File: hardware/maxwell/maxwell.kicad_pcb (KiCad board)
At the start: 2 copper layers, 122 x 59 mm, 99 parts, among them J1 Canbus 1, J10 SPI2_B, J11 BACKUP, J12 UART4, J13 UART5, J14 I2C1, J16 ESP_BM, J17 ESP_PROG, J19 Interconnect (Power), J2 SPI2_C, J20 Interconnect (uC), J3 Neopixel, J4 BOOT0, J5 SPI2_A, J6 Programmer, J7 Dynamo Input, J8 BOOT1, J9 Battery, Q1 BSS138, Q2 PSMN5R4-25YLD, Q3 DMG9926UDM, Q4 NTR1P02T1, Q5 NTR1P02T1, U1 MCP1501, U10 MIC39102, U11 AP9101C-SOT-25, U12 INA219AID, U13 PCF8593, U2 SN65HVD233, U3 TPS2113, U4 PCA9536D, U5 ESP-32S, U6 AD7991, U7 STM32F103RETx, U8 TLP188, U9 Buck Regulator, Y1 32.768k, Y2 8M

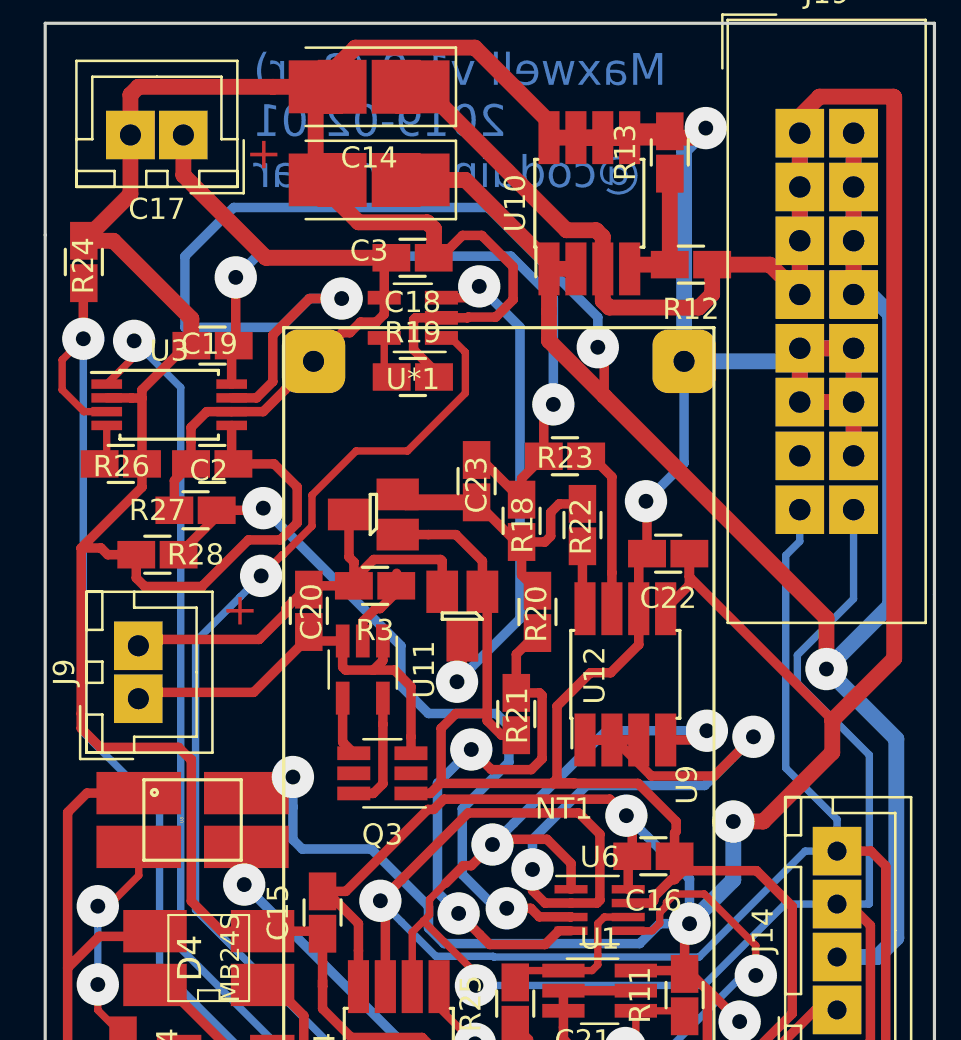
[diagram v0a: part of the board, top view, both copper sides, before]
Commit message: Updating to 1.8b; re-assigns power sources-to-TPS chip reverting earlier changes.
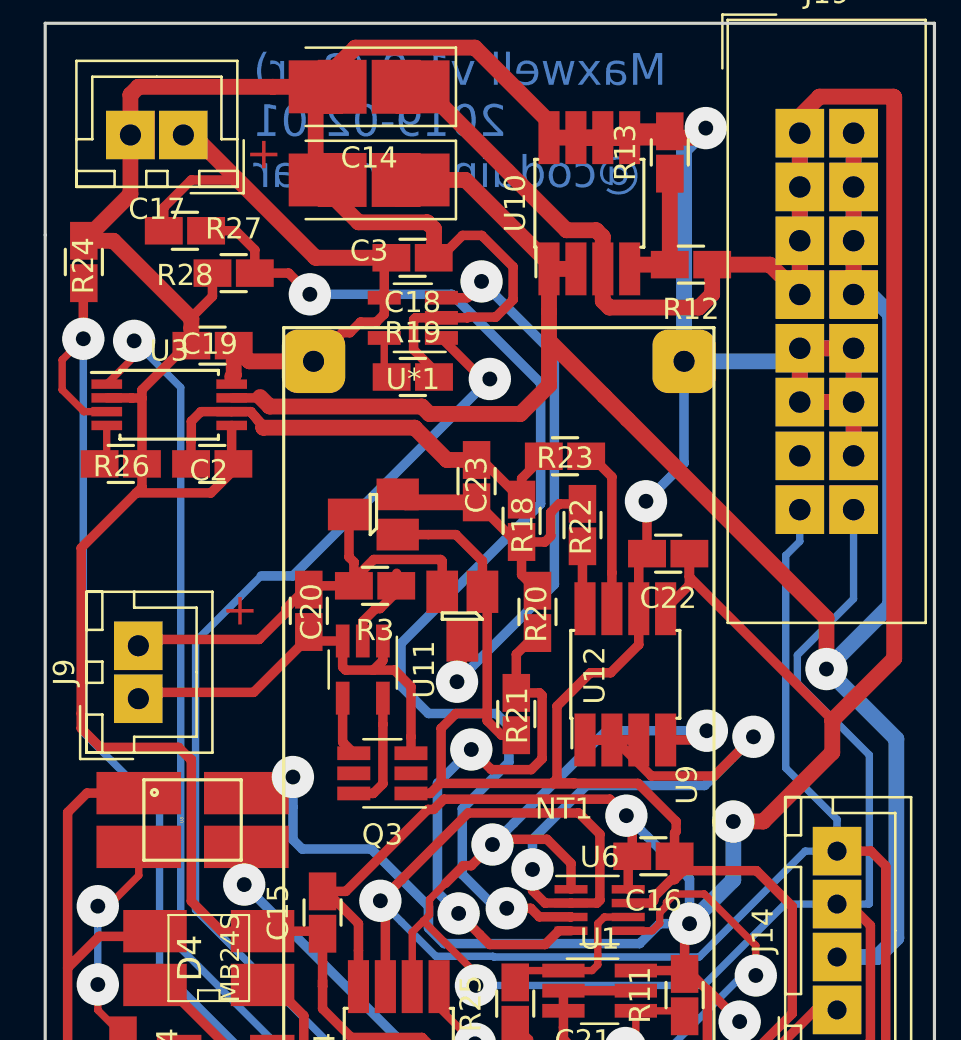
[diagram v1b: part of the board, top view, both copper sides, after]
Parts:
- moved R27 13.8 mm to (65.9, 84.8)
- moved R28 13.2 mm to (63.6, 82.8)
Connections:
- net DISABLE_DYNAMO_SRC renamed DISABLE_BATTERY_SRC
- C19 pad 2: +BATT -> /Power/+Dynamo_Buck
- C2 pad 1: /Power/+Dynamo_Buck -> +BATT
- U3 pad 6: /Power/+Dynamo_Buck -> +BATT
- U3 pad 8: +BATT -> /Power/+Dynamo_Buck
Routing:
- net VCC: track 325.6 -> 297.4 mm, vias 3 -> 1
- net DYNAMO_REG_VOLTAGE: track 35.9 -> 56.2 mm
- net +BATT: track 34.4 -> 23.0 mm, vias 2 -> 0
- net GND: track 771.4 -> 761.8 mm
- net /Power/BATT_CHARGE_PRE_POLARITY: track 24.8 -> 26.6 mm
- net /Power/+Dynamo_Buck: track 31.7 -> 30.0 mm

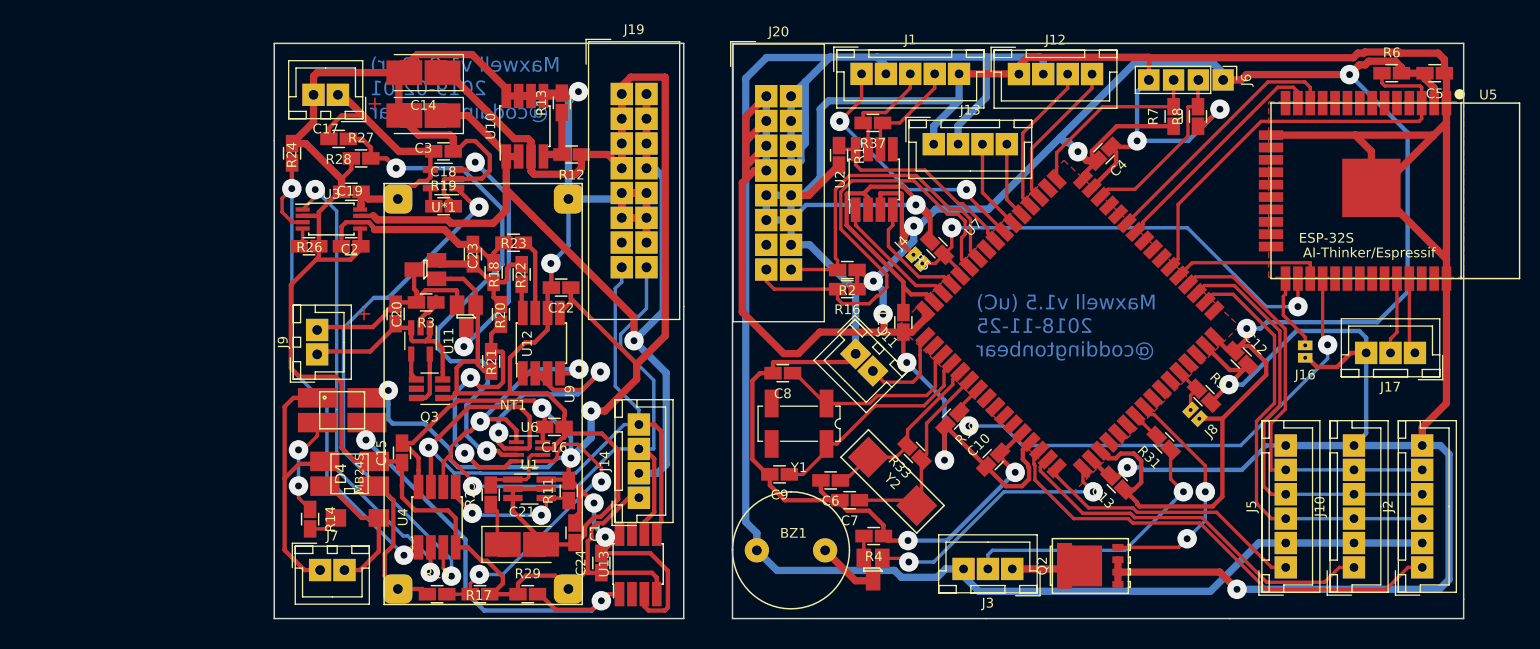
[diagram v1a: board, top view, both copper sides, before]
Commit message: Revision 1.9a
* Separates PCB into three boards (from two); adding a new
  'Rectifier' board mounted directly to the 'Power' board via a
  board-to-board connector.
* Switches to active rectification.
* Provide 5V directly to the battery; drop VCC voltage to
  4.3V via a diode drop.
* Adds new WAKE-controlled power switch to reduce quiescent
  current to, essentially, nil, and remove the need
  carefully managing sleep states of various devices.
* Adds 220uF capacitor to 3V3 output on 'Main' PCB.
* Control power to SPI/I2C connector via a new uC-controlled MOSFET.
* Adds clock chip to main uC board for permanent timekeeping and
  alarm-based wakeup.
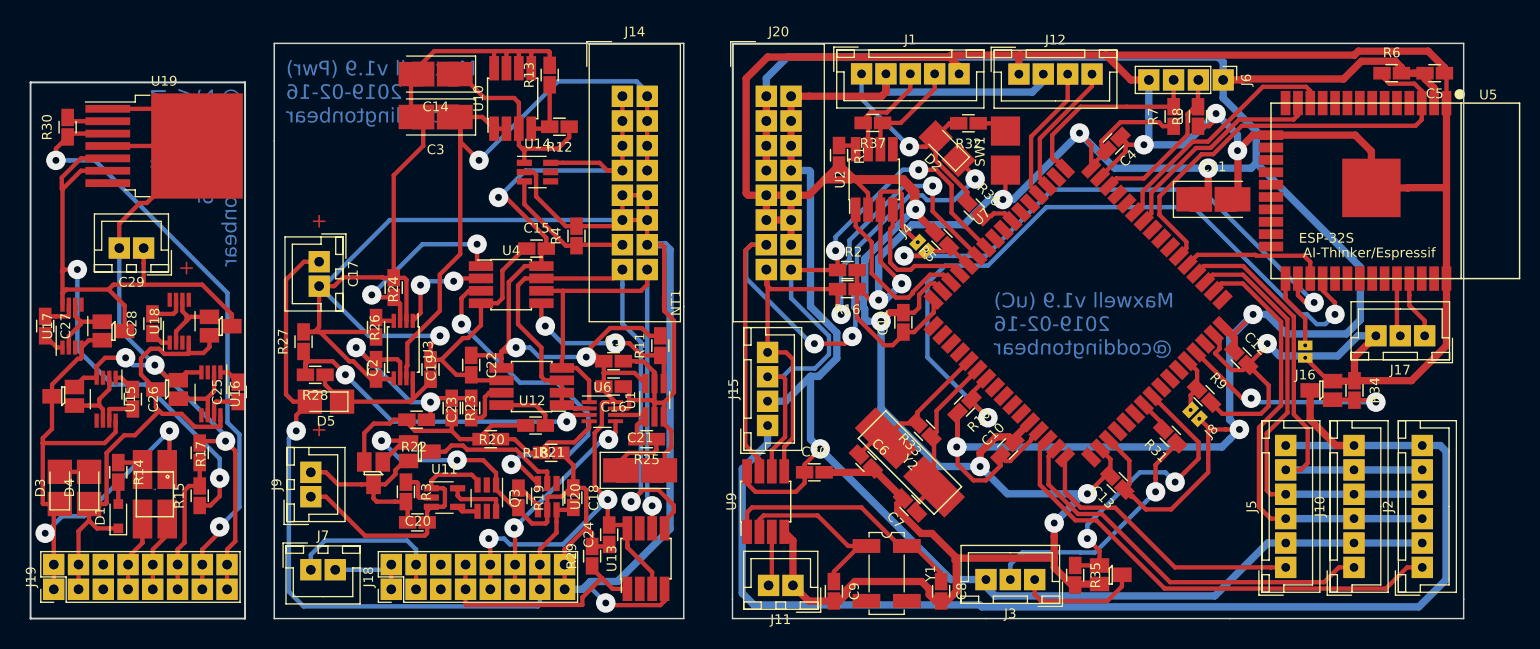
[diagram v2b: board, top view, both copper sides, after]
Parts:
- removed BZ1: Buzzer, coddingtonbear:12mm_buzzer
- removed J13: UART5, coddingtonbear:JST_XH_B04B-XH-A_04x2.50mm_Straight_LargePads
- removed U*1: MCP73831T, Package_TO_SOT_SMD:SOT-23-5_HandSoldering
- added C25: 1u, coddingtonbear:0805_Milling, F.Cu at (53.2, 108.8)
- added C26: 1u, coddingtonbear:0805_Milling, F.Cu at (42.5, 109.5)
- added C27: 1u, coddingtonbear:0805_Milling, F.Cu at (33.5, 102.0)
- added C28: 1u, coddingtonbear:0805_Milling, F.Cu at (44.5, 101.8)
- added C29: 6000uF, coddingtonbear:JST_XH_B02B-XH-A_02x2.50mm_Straight_LargePads, F.Cu at (43.6, 94.0)
- added C30: 0.1u, coddingtonbear:0805_Milling, F.Cu at (112.4, 117.0)
- added C31: 220u, coddingtonbear:CP_Tantalum_Case-C_EIA-6032-28_Milling, F.Cu at (153.3, 89.0)
- added D2: MBR1020VL, coddingtonbear:D_SOD-123_LargePads, F.Cu at (126.0, 83.8)
- added D3: 18V, coddingtonbear:D_SOD-123_LargePads, F.Cu at (35.0, 118.6)
- added D5: GS1M-LTP, coddingtonbear:D_SOD-123_LargePads, F.Cu at (62.3, 109.8)
- added J15: I2C1, coddingtonbear:JST_XH_B04B-XH-A_04x2.50mm_Straight_LargePads, F.Cu at (107.6, 112.2)
- added J18: Interconnect (Power-Rect), coddingtonbear:PinHeader_2x08_P2.54mm_Vertical_LargePads, F.Cu at (69.0, 129.0)
- added Q6: DMG2302UK, coddingtonbear:SOT-23_LargePads, F.Cu at (35.4, 109.2)
- added Q7: DMG2302UK, coddingtonbear:SOT-23_LargePads, F.Cu at (46.0, 108.5)
- added Q8: DMG2302UK, coddingtonbear:SOT-23_LargePads, F.Cu at (40.5, 102.5)
- added Q9: DMG2302UK, coddingtonbear:SOT-23_LargePads, F.Cu at (51.5, 102.0)
- added R30: 92k, coddingtonbear:0805_Milling, F.Cu at (35.8, 81.6)
- added R32: 10k, coddingtonbear:0805_Milling, F.Cu at (128.2, 81.2)
- added R34: 10k, coddingtonbear:0805_Milling, F.Cu at (167.8, 108.6)
- added R35: 10k, coddingtonbear:0805_Milling, F.Cu at (139.2, 127.5)
- added R36: 10k, coddingtonbear:0805_Milling, F.Cu at (128.8, 90.0)
- added SW1: SW_Push, coddingtonbear:SMD_MINI_BLACK_TACTILE_SWITCH, F.Cu at (132.0, 84.0)
- added U14: TPS22917, Package_TO_SOT_SMD:SOT-23-6_Handsoldering, F.Cu at (84.0, 86.2)
- added U15: LM74670-Q1, Package_SO:VSSOP-8_3.0x3.0mm_P0.65mm, F.Cu at (39.8, 109.5)
- added U16: LM74670-Q1, Package_SO:VSSOP-8_3.0x3.0mm_P0.65mm, F.Cu at (50.5, 109.0)
- added U17: LM74670-Q1, Package_SO:VSSOP-8_3.0x3.0mm_P0.65mm, F.Cu at (36.2, 102.0)
- added U18: LM74670-Q1, Package_SO:VSSOP-8_3.0x3.0mm_P0.65mm, F.Cu at (47.2, 101.5)
- added U19: LT3086IR, Package_TO_SOT_SMD:TO-263-7_TabPin4, F.Cu at (45.7, 83.5)
- added U20: BQ21040DBVT, Package_TO_SOT_SMD:SOT-23-6_Handsoldering, F.Cu at (85.0, 119.5)
- D1: value GS1M-LTP -> 1N4148WS; footprint coddingtonbear:DO-214AC -> Diode_SMD:D_SOD-323_HandSoldering
- D4: value MB24S -> 18V; footprint coddingtonbear:SO-4_Milling -> coddingtonbear:D_SOD-123_LargePads
- J14: value I2C1 -> Interconnect (Power); footprint coddingtonbear:JST_XH_B04B-XH-A_04x2.50mm_Straight_LargePads -> coddingtonbear:IDC-Header_2x08_P2.54mm_Vertical_Largepads
- J19: value Interconnect (Power) -> Interconnect (Rect); footprint coddingtonbear:IDC-Header_2x08_P2.54mm_Vertical_Largepads -> coddingtonbear:PinHeader_2x08_P2.54mm_Vertical_LargePads
- J7: value Dynamo Input -> Dynamo
- Q1: value BSS138 -> DMG2302UK
- Q2: value PSMN5R4-25YLD -> DMG2302UK; footprint coddingtonbear:PSMN5R4-25YLD -> coddingtonbear:SOT-23_LargePads
- R14: value 200 -> 1k
- R19: value 2k -> ~1.8k
- R4: value >35 -> 10k
- U7: footprint kicad-castellated-breakouts:QFP64-1.27MM-CASTELLATED -> castellated-breakouts:QFP64-1.27MM-CASTELLATED
- U9: value Buck Regulator -> MCP79411-I/SN; footprint coddingtonbear:BOOST_LM2596_3A -> coddingtonbear:SOIC-8_3.9x4.9mm_P1.27mm_LargePads
- Y2: footprint coddingtonbear:Abracon-ABM2 -> coddingtonbear:Abracon-ABM2_LargePads
- moved J19 77.3 mm to (34.4, 129.0), turned to 90 degrees
- moved Q1 49.5 mm to (164.4, 108.6), turned to 180 degrees
- moved R4 43.3 mm to (88.0, 92.8), turned to 90 degrees
- moved J14 41.2 mm to (92.7, 78.4), turned to 0 degrees
- moved C18 37.9 mm to (87.7, 119.6), turned to 270 degrees
- moved R17 32.2 mm to (49.4, 115.0), turned to 270 degrees
- moved U9 31.0 mm to (107.4, 120.0)
- moved R19 30.9 mm to (82.0, 119.6), turned to 270 degrees
- moved C8 27.6 mm to (125.4, 129.2), turned to 270 degrees
- moved D4 26.8 mm to (38.0, 118.6)
- moved R15 26.4 mm to (49.4, 119.4), turned to 90 degrees
- moved C15 25.1 mm to (83.9, 94.0), turned to 0 degrees
- moved U4 25.0 mm to (81.3, 97.8), turned to 0 degrees
- moved J11 24.6 mm to (110.2, 128.6), turned to 180 degrees
- moved D1 24.5 mm to (41.0, 121.5), turned to 90 degrees
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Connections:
- net GNDPWR renamed Net-(J3-Pad1)
- C1 pad 1: +3V3 -> +3V3_A
- C10 pad 1: +3V3 -> +3V3_B
- C10 pad 2: GND -> GND_B
- C11 pad 1: +3V3 -> +3V3_B
- C11 pad 2: GND -> GND_B
- C12 pad 1: +3V3 -> +3V3_B
- C12 pad 2: GND -> GND_B
- C13 pad 1: +3V3 -> +3V3_B
- C13 pad 2: GND -> GND_B
- C14 pad 1: +3V3 -> Net-(C14-Pad1)
- C14 pad 2: GND -> GND_A
- C15 pad 1: GND -> GND_A
- C15 pad 2: +3V3 -> +3V3_A
- C16 pad 2: +3V3 -> +3V3_A
- C17 pad 1: /Power/+Dynamo_Buck -> VDYN
- C17 pad 2: GND -> GND_A
- C18 pad 1: GND -> GND_A
- C18 pad 2: /Power/+Dynamo_Buck -> VDYN
- C19 pad 1: GND -> GND_A
- C19 pad 2: /Power/+Dynamo_Buck -> /Power/4V3
- C2 pad 2: GND -> GND_A
- C22 pad 1: +3V3 -> +3V3_A
- C22 pad 2: GND -> GND_A
- C24 pad 1: GND -> GND_A
- C24 pad 2: +3V3 -> +3V3_A
- C3 pad 1: VCC -> VCC_A
- C3 pad 2: GND -> GND_A
- C4 pad 1: GND -> GND_B
- C4 pad 2: +3V3 -> +3V3_B
- C5 pad 1: GND -> GND_B
- C5 pad 2: +3V3 -> +3V3_B
- C6 pad 2: GND -> GND_B
- C7 pad 2: GND -> GND_B
- C8 pad 2: GND -> GND_B
- C9 pad 2: GND -> GND_B
- D1 pad 1: DYNAMO_NEUTRAL -> V_AC-
- D4 pad 1: /Power/+Dynamo -> V_AC-
- D4 pad 2: GND -> Net-(D3-Pad2)
- J1 pad 1: POWER_ON -> WAKE_B_SIG
- J1 pad 2: VCC -> VCC_B
- J1 pad 5: GND -> GND_B
- J10 pad 2: VCC -> VCC_B
- J10 pad 6: GND -> /GNDAUX
- J11 pad 1: GND -> GND_B
- J12 pad 1: GND -> GND_B
- J12 pad 2: VCC -> VCC_B
- J14 pad 1: GND -> +3V3_A
- J14 pad 2: VCC -> VCC_A
- J14 pad 3: I2C1_SCL -> +3V3_A
- J14 pad 4: I2C1_SDA -> VCC_A
- J16 pad 1: GND -> GND_B
- J17 pad 3: GND -> GND_B
- J19 pad 1: +3V3 -> V_AC+
- J19 pad 10: GND -> +3V3_C
- J19 pad 11: GND -> DYNAMO_VOLTAGE_C
- J19 pad 12: GND -> DYNAMO_VOLTAGE_C
- J19 pad 13: Net-(J19-Pad13) -> VDYN_C
- J19 pad 14: GND -> VDYN_C
- J19 pad 15: I2C1_SDA -> GND_C
- J19 pad 16: I2C1_SCL -> GND_C
- J19 pad 2: VCC -> V_AC+
- J19 pad 3: +3V3 -> V_AC-
- J19 pad 4: VCC -> V_AC-
- J19 pad 5: +3V3 -> Net-(J19-Pad5)
- J19 pad 6: VCC -> Net-(J19-Pad6)
- J19 pad 7: +3V3 -> DYNAMO_POLE_SIG_C
- J19 pad 8: VCC -> DYNAMO_POLE_SIG_C
- J19 pad 9: GND -> +3V3_C
- J2 pad 2: VCC -> VCC_B
- J2 pad 6: GND -> /GNDAUX
- J20 pad 1: +3V3 -> +3V3_B
- J20 pad 10: GND -> GND_B
- J20 pad 11: GND -> GND_B
- J20 pad 12: GND -> GND_B
- J20 pad 13: Net-(J20-Pad13) -> WAKE_B
- J20 pad 14: GND -> GND_B
- J20 pad 15: I2C1_SDA -> I2C1_SDA_B
- J20 pad 16: I2C1_SCL -> I2C1_SCL_B
- J20 pad 2: VCC -> VCC_B
- J20 pad 3: +3V3 -> +3V3_B
- J20 pad 4: VCC -> VCC_B
- J20 pad 5: +3V3 -> +3V3_B
- J20 pad 6: VCC -> VCC_B
- J20 pad 7: +3V3 -> +3V3_B
- J20 pad 8: VCC -> VCC_B
- J20 pad 9: GND -> GND_B
- J3 pad 3: VCC -> VCC_B
- J4 pad 1: +3V3 -> +3V3_B
- J5 pad 2: VCC -> VCC_B
- J5 pad 6: GND -> /GNDAUX
- J6 pad 1: +3V3 -> +3V3_B
- J6 pad 4: GND -> GND_B
- J7 pad 2: DYNAMO_NEUTRAL -> Net-(J18-Pad1)
- J8 pad 1: +3V3 -> +3V3_B
- NT1 pad 1: GNDA -> GND_A
- NT1 pad 2: GND -> GNDA
- Q1 pad 1: BUZZER -> ENABLE_AUX
- Q1 pad 2: Net-(Q1-Pad2) -> GND_B
- Q1 pad 3: Net-(BZ1-Pad2) -> /GNDAUX
- Q2 pad 1: GND -> ENABLE_LEDS
- Q2 pad 2: ENABLE_BATT_POWER -> GND_B
- Q3 pad 1: GND -> GND_A
- Q4 pad 1: GND -> GND_A
- Q5 pad 1: GND -> GND_A
- R1 pad 1: CAN_DISABLE -> Net-(R1-Pad1)
- R1 pad 2: GND -> GND_B
- R10 pad 2: +3V3 -> +3V3_B
- R11 pad 2: +3V3 -> +3V3_A
- R12 pad 1: +3V3 -> Net-(C14-Pad1)
- R13 pad 2: GND -> GND_A
- R15 pad 1: /Power/+Dynamo -> Net-(C29-Pad1)
- R15 pad 2: DYNAMO_VOLTAGE -> DYNAMO_VOLTAGE_C
- R16 pad 1: +3V3 -> +3V3_B
- R16 pad 2: I2C1_SDA -> I2C1_SDA_B
- R17 pad 1: GND -> GND_C
- R17 pad 2: DYNAMO_VOLTAGE -> DYNAMO_VOLTAGE_C
- R19 pad 2: GND -> GND_A
- R2 pad 1: +3V3 -> +3V3_B
- R2 pad 2: I2C1_SCL -> I2C1_SCL_B
- R21 pad 2: GND -> GND_A
- R24 pad 1: GND -> GND_A
- R26 pad 1: GND -> GND_A
- R27 pad 1: GND -> DYNAMO_REG_VOLTAGE
- R27 pad 2: DYNAMO_REG_VOLTAGE -> GND_A
- R28 pad 1: DYNAMO_REG_VOLTAGE -> /Power/4V3
- R28 pad 2: /Power/+Dynamo_Buck -> DYNAMO_REG_VOLTAGE
- R29 pad 1: GND -> DYNAMO_POLE_SIG
- R29 pad 2: Net-(R29-Pad2) -> GND_A
- R4 pad 1: GND -> WAKE_A
- R4 pad 2: Net-(Q1-Pad2) -> GND_A
- R5 pad 2: GND -> GND_B
- R6 pad 2: +3V3 -> +3V3_B
- R7 pad 1: +3V3 -> +3V3_B
- R8 pad 1: GND -> GND_B
- R9 pad 2: GND -> GND_B
- U1 pad 6: +3V3 -> +3V3_A
- U10 pad 1: VCC -> VCC_A
- U10 pad 2: VCC -> VCC_A
- U10 pad 3: +3V3 -> Net-(C14-Pad1)
- U10 pad 5: GND -> GND_A
- U10 pad 6: GND -> GND_A
- U10 pad 7: GND -> GND_A
- U10 pad 8: GND -> GND_A
- U12 pad 1: I2C1_SDA -> I2C1_SDA_A
- U12 pad 2: I2C1_SDA -> I2C1_SDA_A
- U12 pad 3: I2C1_SDA -> I2C1_SDA_A
- U12 pad 4: I2C1_SCL -> I2C1_SCL_A
- U12 pad 5: +3V3 -> +3V3_A
- U12 pad 6: GND -> GND_A
- U13 pad 1: Net-(R29-Pad2) -> DYNAMO_POLE_SIG
- U13 pad 3: +3V3 -> +3V3_A
- U13 pad 4: GND -> GND_A
- U13 pad 5: I2C1_SDA -> I2C1_SDA_A
- U13 pad 6: I2C1_SCL -> I2C1_SCL_A
- U13 pad 8: +3V3 -> +3V3_A
- U2 pad 2: GND -> GND_B
- U2 pad 3: +3V3 -> +3V3_B
- U2 pad 8: CAN_DISABLE -> Net-(R1-Pad1)
- U3 pad 2: GND -> GND_A
- U3 pad 5: GND -> GND_A
- U3 pad 7: VCC -> VCC_A
- U3 pad 8: /Power/+Dynamo_Buck -> /Power/4V3
- U4 pad 4: GND -> GND_A
- U4 pad 6: I2C1_SCL -> I2C1_SCL_A
- U4 pad 7: I2C1_SDA -> I2C1_SDA_A
- U4 pad 8: +3V3 -> +3V3_A
- U5 pad 1: GND -> GND_B
- U5 pad 15: GND -> GND_B
- U5 pad 2: +3V3 -> +3V3_B
- U5 pad 38: GND -> GND_B
- U5 pad 39: GND -> GND_B
- U6 pad 1: I2C1_SCL -> I2C1_SCL_A
- U6 pad 2: I2C1_SDA -> I2C1_SDA_A
- U6 pad 8: +3V3 -> +3V3_A
- U7 pad 1: +BACKUP -> Net-(U7-Pad1)
- U7 pad 12: GND -> GND_B
- U7 pad 13: +3V3 -> +3V3_B
- U7 pad 17: BUZZER -> Net-(U7-Pad17)
- U7 pad 18: GND -> GND_B
- U7 pad 19: +3V3 -> +3V3_B
- U7 pad 24: ENABLE_BATT_POWER -> ENABLE_LEDS
- U7 pad 29: Net-(U7-Pad29) -> ENABLE_AUX
- U7 pad 3: Net-(C8-Pad1) -> Net-(U7-Pad3)
- U7 pad 31: GND -> GND_B
- U7 pad 32: +3V3 -> +3V3_B
- U7 pad 4: Net-(C9-Pad1) -> Net-(U7-Pad4)
- U7 pad 47: GND -> GND_B
- U7 pad 48: +3V3 -> +3V3_B
- U7 pad 55: POWER_ON -> Net-(R36-Pad2)
- U7 pad 58: I2C1_SCL -> I2C1_SCL_B
- U7 pad 59: I2C1_SDA -> I2C1_SDA_B
- U7 pad 63: GND -> GND_B
- U7 pad 64: +3V3 -> +3V3_B
- U8 pad 1: DYNAMO_AC -> V_AC+
- U8 pad 4: Net-(R29-Pad2) -> DYNAMO_POLE_SIG_C
- U8 pad 6: +3V3 -> +3V3_C
- U9 pad 1: /Power/+Dynamo -> Net-(C8-Pad1)
- U9 pad 2: GND -> Net-(C9-Pad1)
- U9 pad 3: /Power/+Dynamo_Buck -> +BACKUP
- U9 pad 4: GND -> GND_B
- Y1 pad 1: Net-(C8-Pad1) -> Net-(C9-Pad1)
- Y1 pad 4: Net-(C9-Pad1) -> Net-(C8-Pad1)
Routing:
- net GND: track 761.8 -> 0.00 mm, vias 10 -> 0
- net +3V3: track 502.5 -> 0.00 mm, vias 14 -> 0
- net GND_B: track 0.00 -> 453.0 mm, vias 0 -> 9
- net +3V3_B: track 0.00 -> 339.5 mm, vias 0 -> 8
- net GND_A: track 0.00 -> 304.0 mm, vias 0 -> 4
- net VCC: track 297.4 -> 0.00 mm, vias 1 -> 0
- net VCC_B: track 0.00 -> 160.4 mm, vias 0 -> 1
- net I2C1_SDA: track 153.2 -> 0.00 mm, vias 3 -> 0
- net /GNDAUX: track 0.00 -> 130.7 mm
- net +3V3_A: track 0.00 -> 130.0 mm, vias 0 -> 5
- net I2C1_SCL: track 117.7 -> 0.00 mm, vias 3 -> 0
- net GND_C: track 0.00 -> 93.3 mm, vias 0 -> 3
- net Net-(C29-Pad1): track 0.00 -> 88.3 mm, vias 0 -> 2
- net VDYN: track 0.00 -> 77.7 mm, vias 0 -> 1
- net WAKE_B: track 0.00 -> 72.3 mm, vias 0 -> 3
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- removed copper zone on F.Cu, net GND
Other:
- board size 122 x 59 mm -> 147 x 59 mm
- board text added: "Maxwell v1.9 (Pwr) 2019-02-16 @coddingtonbear"
- board text added: "Maxwell v1.9 (Rect) 2019-02-16 @coddingtonbear"
- board text added: "Maxwell v1.9 (uC) 2019-02-16 @coddingtonbear"
- board text removed: "Maxwell v1.5 (uC) 2018-11-25 @coddingtonbear"
- board text removed: "Maxwell v1.8 (Pwr) 2019-02-01 @coddingtonbear"

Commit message: Missing connection from diode controller to VDYN+; bodged.
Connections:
- U18 pad 8: Net-(U18-Pad8) -> Net-(C29-Pad1)
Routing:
- net Net-(C29-Pad1): track 88.3 -> 90.0 mm

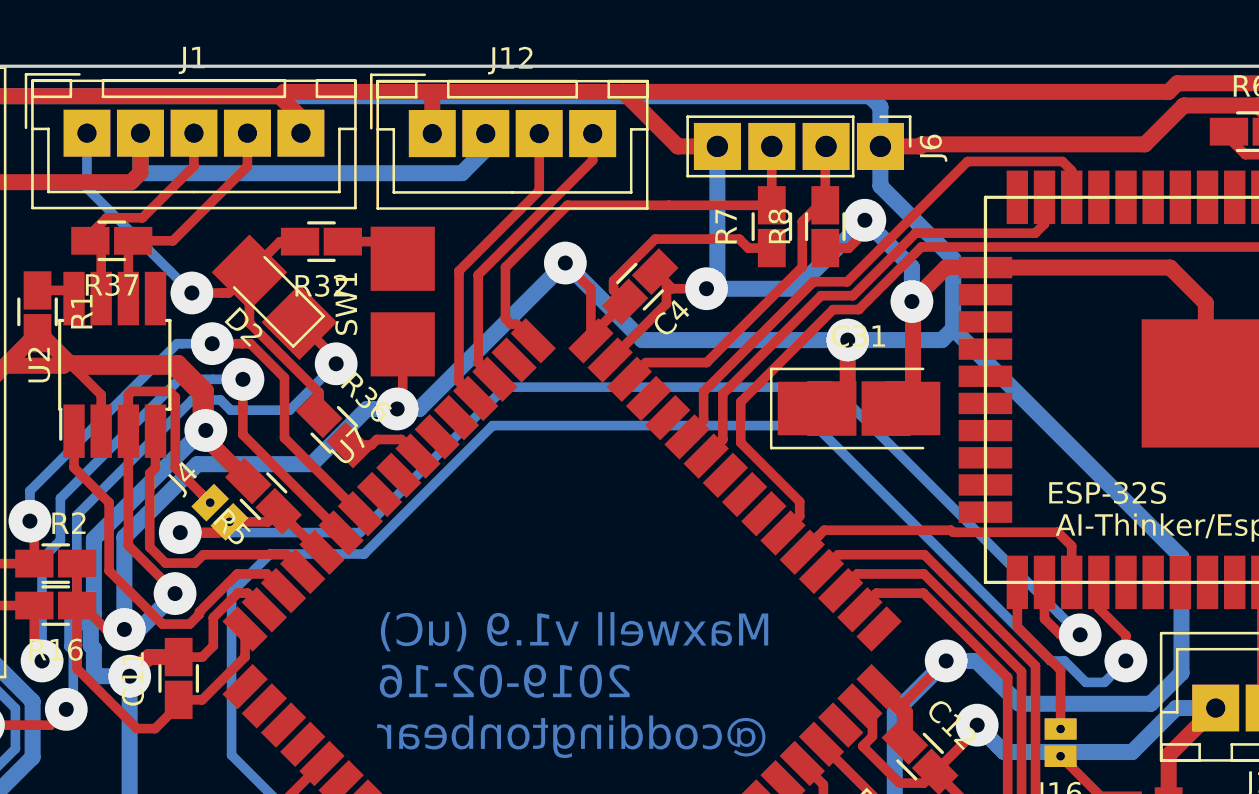
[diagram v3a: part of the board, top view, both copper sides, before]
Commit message: Fixing errata:
* Connecting ESP32 to WAKE to ensure that the ESP32 can keep
  the power on while doing things like flashing the uC.
* Pull power button high to VCC via a diode instead of
  3V3 which is the very thing the power button will be
  turning on.
* Updating sense resistor to 100mOhm instead of 20mOhm.
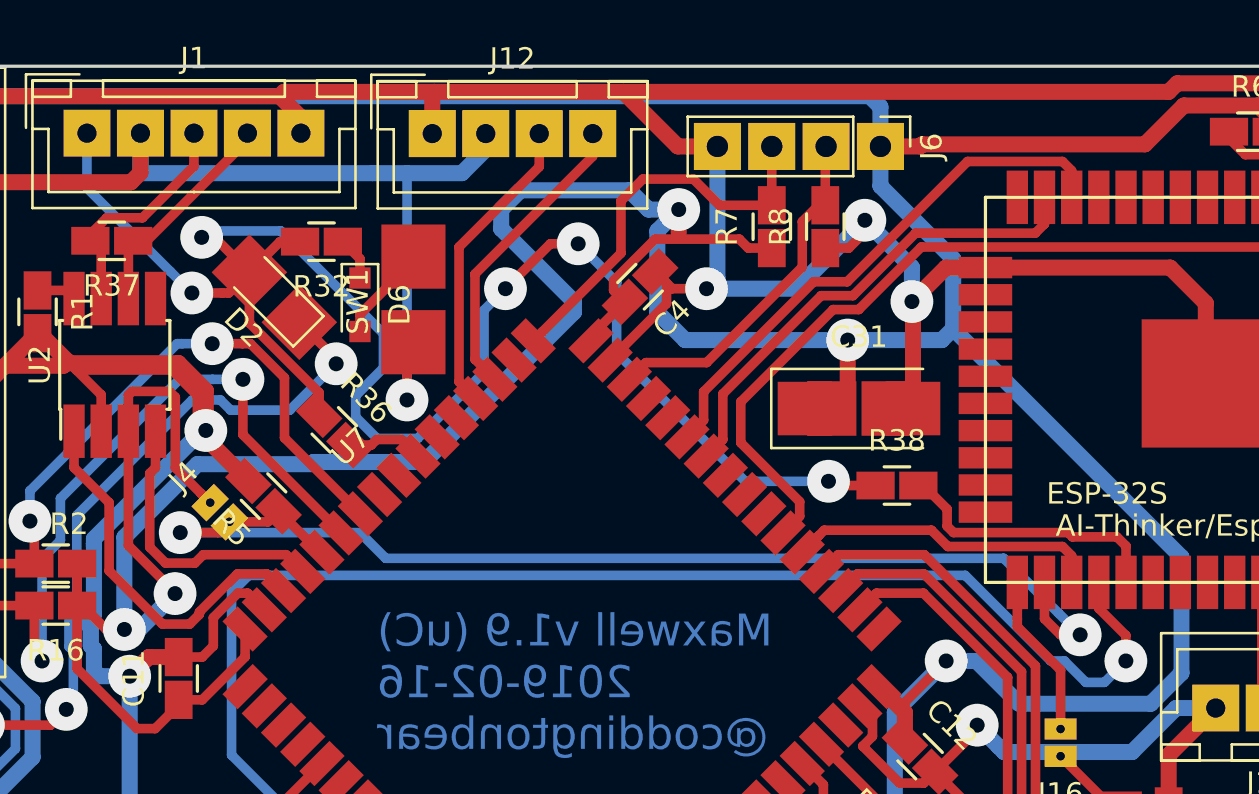
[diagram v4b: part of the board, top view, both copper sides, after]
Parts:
- added D6: D, Diode_SMD:D_SOD-323_HandSoldering, F.Cu at (130.0, 84.2)
- added R38: 300, coddingtonbear:0805_Milling, F.Cu at (155.1, 92.6)
- R22: value 0.02 -> 0.1
- moved SW1 0.51 mm to (132.5, 83.9)
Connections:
- net WAKE_B_SIG renamed ESP_AVAILABLE
- R32 pad 1: Net-(R32-Pad1) -> Net-(D6-Pad1)
- SW1 pad 1: Net-(R32-Pad1) -> Net-(D6-Pad2)
- SW1 pad 2: +3V3_B -> VCC_B
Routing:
- net ESP_AVAILABLE: track 23.6 -> 78.3 mm, vias 1 -> 5
- net VCC_B: track 160.4 -> 173.9 mm, vias 1 -> 2
- net Net-(R38-Pad2): track 0.00 -> 13.0 mm
- net +3V3_B: track 339.5 -> 350.5 mm, vias 8 -> 7
- net N_RST: track 76.3 -> 70.5 mm
- net BOOT0: track 61.2 -> 55.5 mm
- net Net-(D6-Pad2): track 0.00 -> 4.62 mm
- net Net-(R32-Pad1): track 3.13 -> 0.00 mm
- net Net-(D6-Pad1): track 0.00 -> 2.03 mm
- net SWCLK: track 20.5 -> 19.0 mm
- net /CAN-: track 11.1 -> 10.4 mm
